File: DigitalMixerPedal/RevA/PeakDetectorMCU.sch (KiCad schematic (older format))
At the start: 14 parts, among them J7 Conn_01x05, U11 STM32F051K8Tx

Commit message: hw update
RevA layout completed (draft)
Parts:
- J7: footprint (none) -> Connector_PinHeader_2.54mm:PinHeader_1x05_P2.54mm_Vertical
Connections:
- net PEAK_OUT_PWM1: now also U11.27 (PB4); no longer U11.12 (PA6)
- net PEAK_OUT_PWM2: now also U11.28 (PB5); no longer U11.13 (PA7)
- net PEAK_OUT_PWM3: now also U11.14 (PB0); no longer U11.18 (PA8)
- net PEAK_OUT_PWM4: now also U11.15 (PB1); no longer U11.19 (PA9)
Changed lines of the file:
@@
 SYS_SWDIO
 Wire Wire Line
-	6875 2800 7175 2800
-Wire Wire Line
-	6875 2900 7175 2900
-Wire Wire Line
-	6875 3000 7175 3000
-Wire Wire Line
-	6875 3100 7175 3100
+	5775 3400 5475 3400
+Wire Wire Line
+	5775 3500 5475 3500
+Wire Wire Line
+	5775 3100 5475 3100
+Wire Wire Line
+	5775 3200 5475 3200
 NoConn ~ 5775 2800
 NoConn ~ 5775 2900
-NoConn ~ 5775 3100
-NoConn ~ 5775 3200
 NoConn ~ 5775 3300
-NoConn ~ 5775 3400
-NoConn ~ 5775 3500
+NoConn ~ 6875 2800
+NoConn ~ 6875 2900
 NoConn ~ 5775 3600
 NoConn ~ 5775 3700
@@
 Text Label 3550 4175 0    50   ~ 0
 PEAK_IN_ADC4
-Text Label 7175 2800 0    50   ~ 0
+Text Label 5475 3400 2    50   ~ 0
 PEAK_OUT_PWM1
-Text Label 7175 2900 0    50   ~ 0
+Text Label 5475 3500 2    50   ~ 0
 PEAK_OUT_PWM2
-Text Label 7175 3000 0    50   ~ 0
+Text Label 5475 3100 2    50   ~ 0
 PEAK_OUT_PWM3
-Text Label 7175 3100 0    50   ~ 0
+Text Label 5475 3200 2    50   ~ 0
 PEAK_OUT_PWM4
 Wire Wire Line
@@
 F 0 "J7" H 5255 6617 50  0000 L CNN
 F 1 "Conn_01x05" H 5255 6526 50  0000 L CNN
-F 2 "" H 5175 6575 50  0001 C CNN
+F 2 "Connector_PinHeader_2.54mm:PinHeader_1x05_P2.54mm_Vertical" H 5175 6575 50  0001 C CNN
 F 3 "~" H 5175 6575 50  0001 C CNN
 	1    5175 6575
@@
 F3 "PEAK_OUT_BUF" I R 3400 2050 50
 $EndSheet
+NoConn ~ 6875 3000
+NoConn ~ 6875 3100
 $EndSCHEMATC

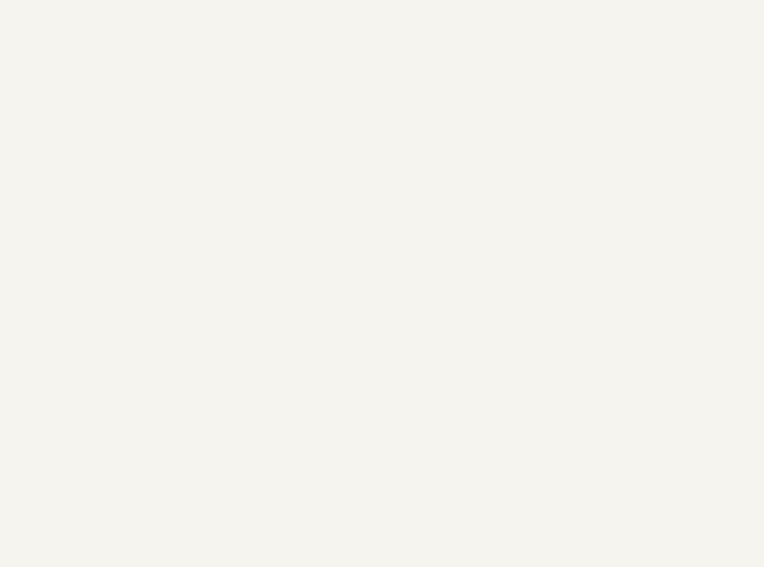
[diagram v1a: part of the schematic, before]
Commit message: updated hw
- added testpoints
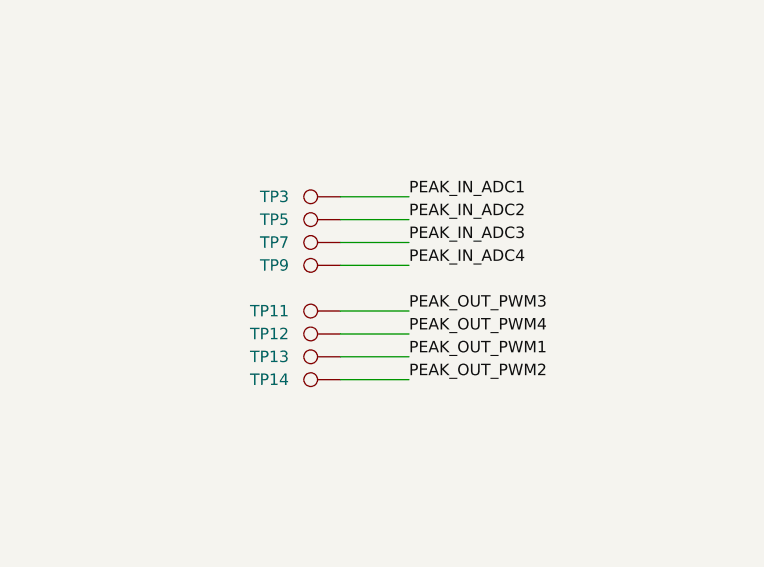
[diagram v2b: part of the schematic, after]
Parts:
- added TP11, TP12, TP13, TP14, TP3, TP5, TP7, TP9: TestPoint, TestPoint:TestPoint_Pad_D1.0mm, symbol Connector:TestPoint
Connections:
- net PEAK_IN_ADC1: now also TP3.1
- net PEAK_IN_ADC2: now also TP5.1
- net PEAK_IN_ADC3: now also TP7.1
- net PEAK_IN_ADC4: now also TP9.1
- net PEAK_OUT_PWM1: now also TP13.1
- net PEAK_OUT_PWM2: now also TP14.1
- net PEAK_OUT_PWM3: now also TP11.1
- net PEAK_OUT_PWM4: now also TP12.1
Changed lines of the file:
@@
 NoConn ~ 6875 3000
 NoConn ~ 6875 3100
+$Comp
+L Connector:TestPoint TP?
+U 1 1 5F72C4BC
+P 8775 5325
+AR Path="/5F6E135D/5F72C4BC" Ref="TP?"  Part="1"
+AR Path="/5F6E91E5/5F72C4BC" Ref="TP?"  Part="1"
+AR Path="/5F6EDB29/5F72C4BC" Ref="TP?"  Part="1"
+AR Path="/5F6F225F/5F72C4BC" Ref="TP?"  Part="1"
+AR Path="/5F74C2DC/5F72C4BC" Ref="TP?"  Part="1"
+AR Path="/5F7234CD/5F72C4BC" Ref="TP3"  Part="1"
+F 0 "TP3" V 8775 5550 50  0000 L CNN
+F 1 "TestPoint" H 8833 5352 50  0001 L CNN
+F 2 "TestPoint:TestPoint_Pad_D1.0mm" H 8975 5325 50  0001 C CNN
+F 3 "~" H 8975 5325 50  0001 C CNN
+	1    8775 5325
+	0    -1   -1   0
+$EndComp
+Wire Wire Line
+	8775 5325 9075 5325
+Text Label 9075 5325 0    50   ~ 0
+PEAK_IN_ADC1
+Text Label 9075 5425 0    50   ~ 0
+PEAK_IN_ADC2
+Text Label 9075 5525 0    50   ~ 0
+PEAK_IN_ADC3
+Text Label 9075 5625 0    50   ~ 0
+PEAK_IN_ADC4
+Text Label 9075 6025 0    50   ~ 0
+PEAK_OUT_PWM1
+Text Label 9075 6125 0    50   ~ 0
+PEAK_OUT_PWM2
+Text Label 9075 5825 0    50   ~ 0
+PEAK_OUT_PWM3
+Text Label 9075 5925 0    50   ~ 0
+PEAK_OUT_PWM4
+$Comp
+L Connector:TestPoint TP?
+U 1 1 5F7373A3
+P 8775 5425
+AR Path="/5F6E135D/5F7373A3" Ref="TP?"  Part="1"
+AR Path="/5F6E91E5/5F7373A3" Ref="TP?"  Part="1"
+AR Path="/5F6EDB29/5F7373A3" Ref="TP?"  Part="1"
+AR Path="/5F6F225F/5F7373A3" Ref="TP?"  Part="1"
+AR Path="/5F74C2DC/5F7373A3" Ref="TP?"  Part="1"
+AR Path="/5F7234CD/5F7373A3" Ref="TP5"  Part="1"
+F 0 "TP5" V 8775 5650 50  0000 L CNN
+F 1 "TestPoint" H 8833 5452 50  0001 L CNN
+F 2 "TestPoint:TestPoint_Pad_D1.0mm" H 8975 5425 50  0001 C CNN
+F 3 "~" H 8975 5425 50  0001 C CNN
+	1    8775 5425
+	0    -1   -1   0
+$EndComp
+Wire Wire Line
+	8775 5425 9075 5425
+$Comp
+L Connector:TestPoint TP?
+U 1 1 5F73915F
+P 8775 5525
+AR Path="/5F6E135D/5F73915F" Ref="TP?"  Part="1"
+AR Path="/5F6E91E5/5F73915F" Ref="TP?"  Part="1"
+AR Path="/5F6EDB29/5F73915F" Ref="TP?"  Part="1"
+AR Path="/5F6F225F/5F73915F" Ref="TP?"  Part="1"
+AR Path="/5F74C2DC/5F73915F" Ref="TP?"  Part="1"
+AR Path="/5F7234CD/5F73915F" Ref="TP7"  Part="1"
+F 0 "TP7" V 8775 5750 50  0000 L CNN
+F 1 "TestPoint" H 8833 5552 50  0001 L CNN
+F 2 "TestPoint:TestPoint_Pad_D1.0mm" H 8975 5525 50  0001 C CNN
+F 3 "~" H 8975 5525 50  0001 C CNN
+	1    8775 5525
+	0    -1   -1   0
+$EndComp
+Wire Wire Line
+	8775 5525 9075 5525
+$Comp
+L Connector:TestPoint TP?
+U 1 1 5F73AF24
+P 8775 5625
+AR Path="/5F6E135D/5F73AF24" Ref="TP?"  Part="1"
+AR Path="/5F6E91E5/5F73AF24" Ref="TP?"  Part="1"
+AR Path="/5F6EDB29/5F73AF24" Ref="TP?"  Part="1"
+AR Path="/5F6F225F/5F73AF24" Ref="TP?"  Part="1"
+AR Path="/5F74C2DC/5F73AF24" Ref="TP?"  Part="1"
+AR Path="/5F7234CD/5F73AF24" Ref="TP9"  Part="1"
+F 0 "TP9" V 8775 5850 50  0000 L CNN
+F 1 "TestPoint" H 8833 5652 50  0001 L CNN
+F 2 "TestPoint:TestPoint_Pad_D1.0mm" H 8975 5625 50  0001 C CNN
+F 3 "~" H 8975 5625 50  0001 C CNN
+	1    8775 5625
+	0    -1   -1   0
+$EndComp
+Wire Wire Line
+	8775 5625 9075 5625
+$Comp
+L Connector:TestPoint TP?
+U 1 1 5F73CE99
+P 8775 5825
+AR Path="/5F6E135D/5F73CE99" Ref="TP?"  Part="1"
+AR Path="/5F6E91E5/5F73CE99" Ref="TP?"  Part="1"
+AR Path="/5F6EDB29/5F73CE99" Ref="TP?"  Part="1"
+AR Path="/5F6F225F/5F73CE99" Ref="TP?"  Part="1"
+AR Path="/5F74C2DC/5F73CE99" Ref="TP?"  Part="1"
+AR Path="/5F7234CD/5F73CE99" Ref="TP11"  Part="1"
+F 0 "TP11" V 8775 6050 50  0000 L CNN
+F 1 "TestPoint" H 8833 5852 50  0001 L CNN
+F 2 "TestPoint:TestPoint_Pad_D1.0mm" H 8975 5825 50  0001 C CNN
+F 3 "~" H 8975 5825 50  0001 C CNN
+	1    8775 5825
+	0    -1   -1   0
+$EndComp
+Wire Wire Line
+	8775 5825 9075 5825
+$Comp
+L Connector:TestPoint TP?
+U 1 1 5F73EF85
+P 8775 5925
+AR Path="/5F6E135D/5F73EF85" Ref="TP?"  Part="1"
+AR Path="/5F6E91E5/5F73EF85" Ref="TP?"  Part="1"
+AR Path="/5F6EDB29/5F73EF85" Ref="TP?"  Part="1"
+AR Path="/5F6F225F/5F73EF85" Ref="TP?"  Part="1"
+AR Path="/5F74C2DC/5F73EF85" Ref="TP?"  Part="1"
+AR Path="/5F7234CD/5F73EF85" Ref="TP12"  Part="1"
+F 0 "TP12" V 8775 6150 50  0000 L CNN
+F 1 "TestPoint" H 8833 5952 50  0001 L CNN
+F 2 "TestPoint:TestPoint_Pad_D1.0mm" H 8975 5925 50  0001 C CNN
+F 3 "~" H 8975 5925 50  0001 C CNN
+	1    8775 5925
+	0    -1   -1   0
+$EndComp
+Wire Wire Line
+	8775 5925 9075 5925
+$Comp
+L Connector:TestPoint TP?
+U 1 1 5F74115F
+P 8775 6025
+AR Path="/5F6E135D/5F74115F" Ref="TP?"  Part="1"
+AR Path="/5F6E91E5/5F74115F" Ref="TP?"  Part="1"
+AR Path="/5F6EDB29/5F74115F" Ref="TP?"  Part="1"
+AR Path="/5F6F225F/5F74115F" Ref="TP?"  Part="1"
+AR Path="/5F74C2DC/5F74115F" Ref="TP?"  Part="1"
+AR Path="/5F7234CD/5F74115F" Ref="TP13"  Part="1"
+F 0 "TP13" V 8775 6250 50  0000 L CNN
+F 1 "TestPoint" H 8833 6052 50  0001 L CNN
+F 2 "TestPoint:TestPoint_Pad_D1.0mm" H 8975 6025 50  0001 C CNN
+F 3 "~" H 8975 6025 50  0001 C CNN
+	1    8775 6025
+	0    -1   -1   0
+$EndComp
+Wire Wire Line
+	8775 6025 9075 6025
+$Comp
+L Connector:TestPoint TP?
+U 1 1 5F7433B2
+P 8775 6125
+AR Path="/5F6E135D/5F7433B2" Ref="TP?"  Part="1"
+AR Path="/5F6E91E5/5F7433B2" Ref="TP?"  Part="1"
+AR Path="/5F6EDB29/5F7433B2" Ref="TP?"  Part="1"
+AR Path="/5F6F225F/5F7433B2" Ref="TP?"  Part="1"
+AR Path="/5F74C2DC/5F7433B2" Ref="TP?"  Part="1"
+AR Path="/5F7234CD/5F7433B2" Ref="TP14"  Part="1"
+F 0 "TP14" V 8775 6350 50  0000 L CNN
+F 1 "TestPoint" H 8833 6152 50  0001 L CNN
+F 2 "TestPoint:TestPoint_Pad_D1.0mm" H 8975 6125 50  0001 C CNN
+F 3 "~" H 8975 6125 50  0001 C CNN
+	1    8775 6125
+	0    -1   -1   0
+$EndComp
+Wire Wire Line
+	8775 6125 9075 6125
 $EndSCHEMATC
